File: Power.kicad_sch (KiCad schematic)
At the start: 39 parts, among them J7 Conn_01x02, Q1 AO3400A, Q2 AO3401A, Q3 AO3401A, U1 TPS62130

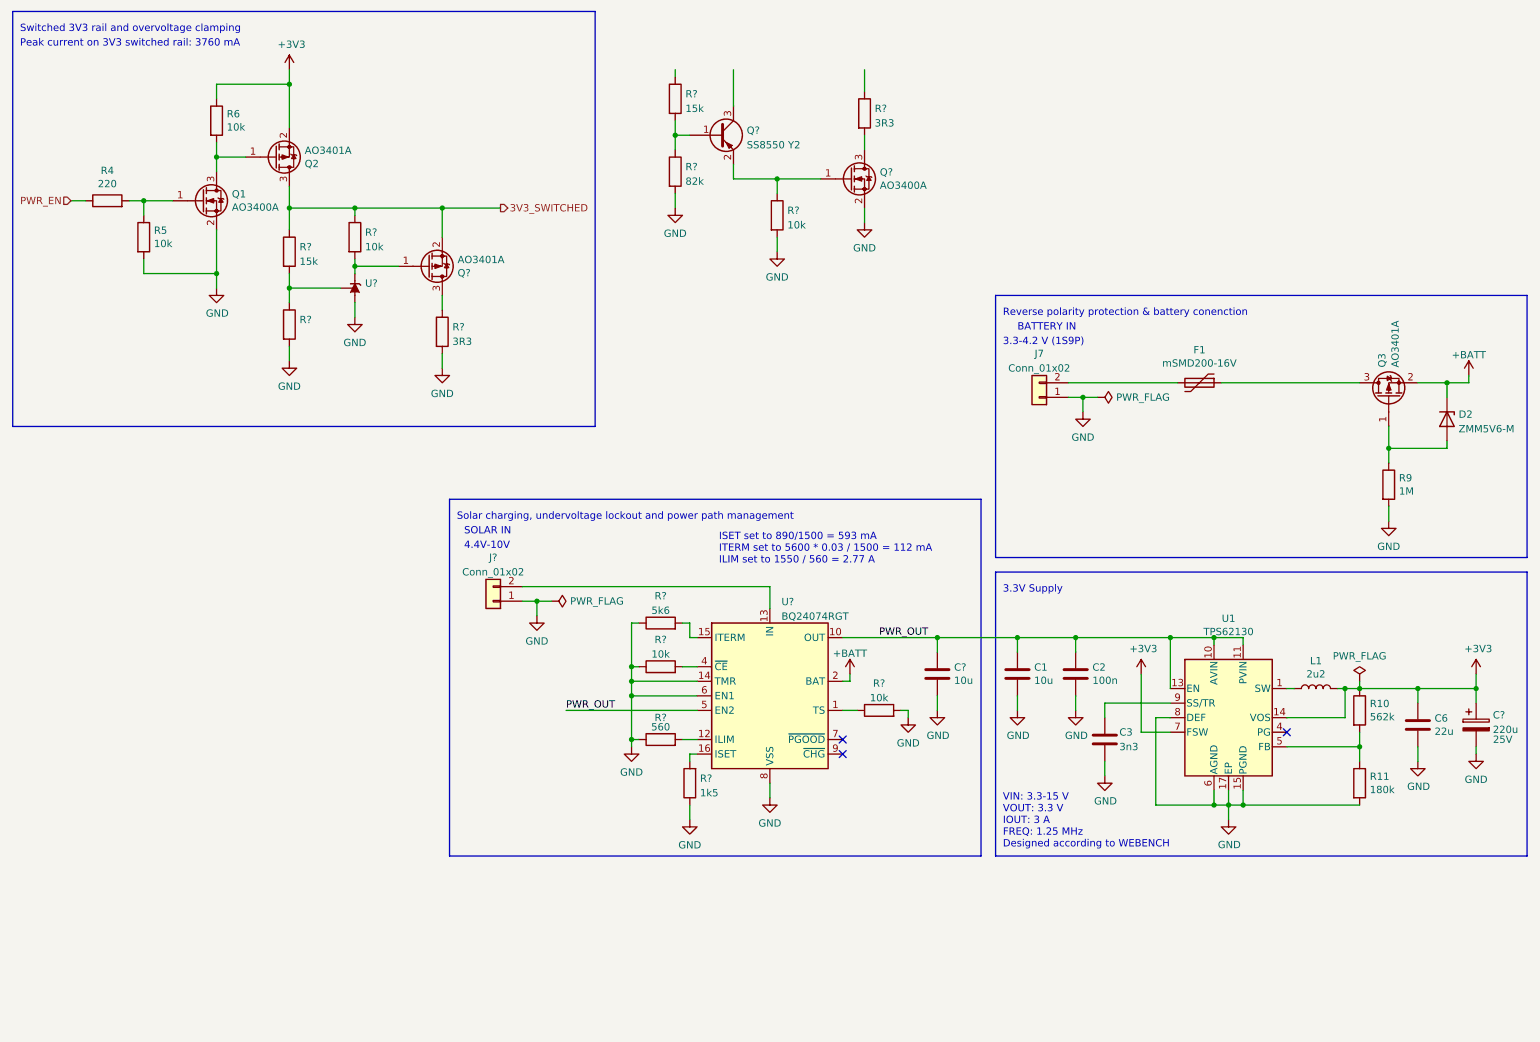
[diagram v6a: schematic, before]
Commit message: Finish rev. 2 schematic and begin PCB layout
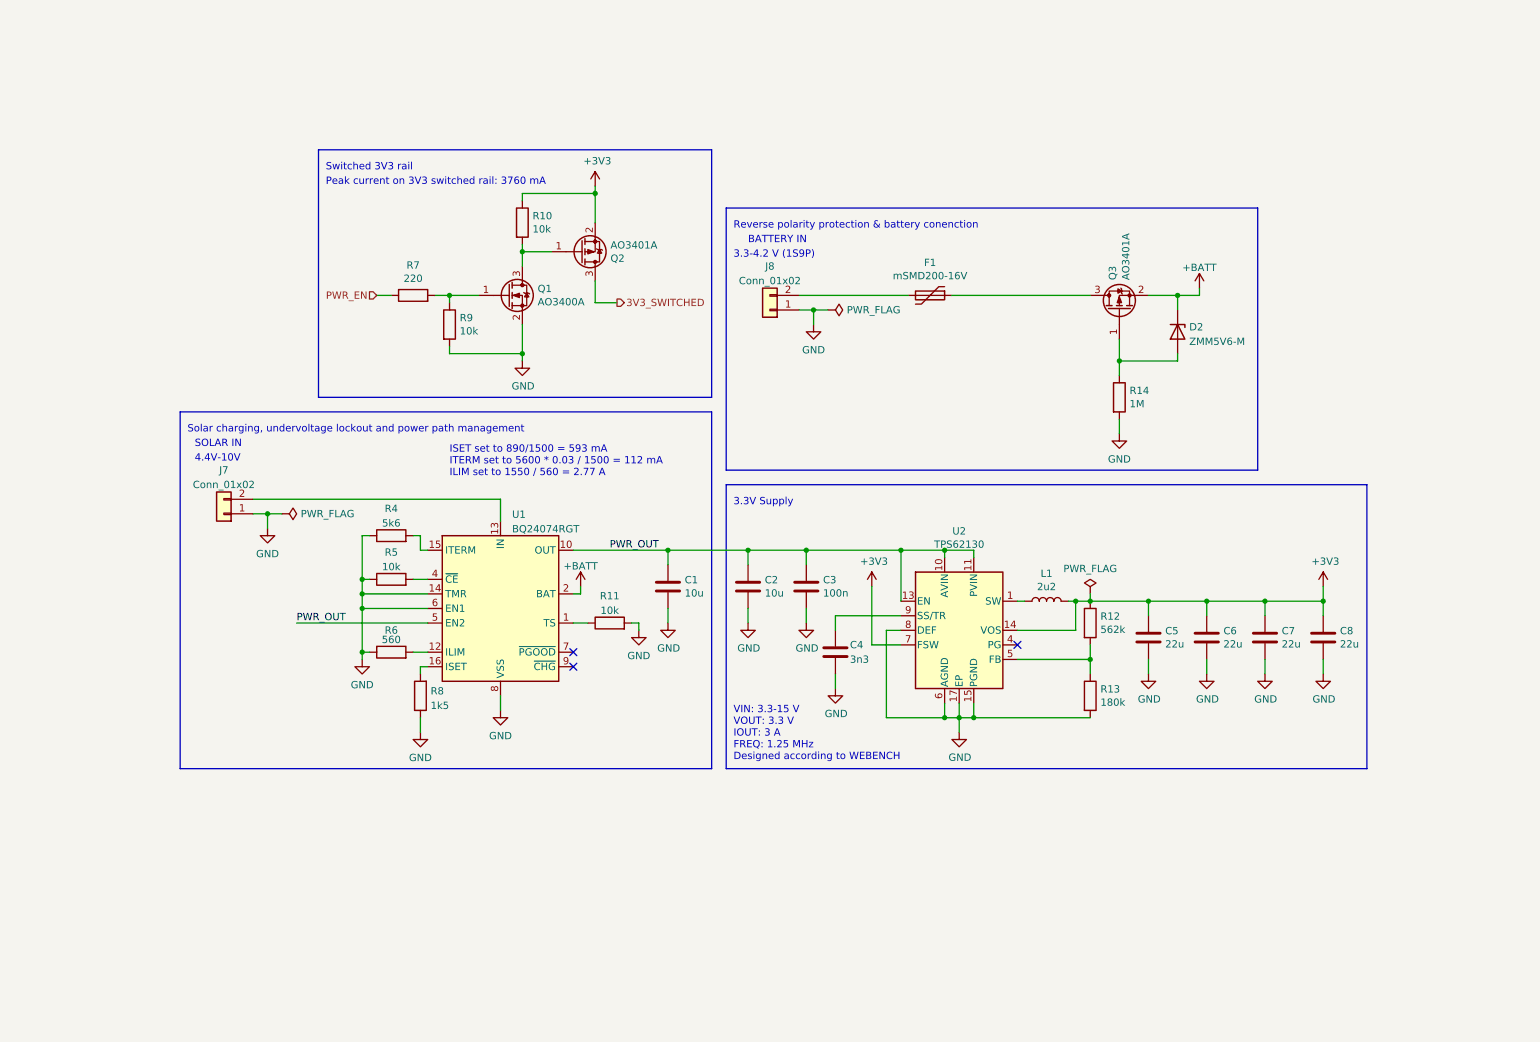
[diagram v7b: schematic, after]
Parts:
- removed C?: 220u, Capacitor_THT:CP_Radial_D8.0mm_P3.50mm, symbol Device:C_Polarized
- removed Q?: SS8550 Y2, symbol Device:Q_PNP_BEC
- removed Q?: AO3400A, Package_TO_SOT_SMD:SOT-23, symbol Transistor_FET:AO3400A
- removed Q?: AO3401A, Package_TO_SOT_SMD:SOT-23, symbol Transistor_FET:AO3401A
- removed R? (x2): 15k, symbol Device:R
- removed R? (x2): 3R3, symbol Device:R
- removed R? (x2): 10k, symbol Device:R
- removed R?: (no value), symbol Device:R
- removed R?: 82k, symbol Device:R
- removed U?: (no value), symbol Reference_Voltage:TL431PK
- added C6, C7, C8: 22u, Capacitor_SMD:C_0805_2012Metric, symbol Device:C
- R11, R5: renamed from R?; footprint (none) -> Resistor_SMD:R_0603_1608Metric; LCSC (none) -> C25804
- R4, R6, R8: renamed from R?; footprint (none) -> Resistor_SMD:R_0603_1608Metric
- gave numbers to parts that had none: 3
- renumbered C1 to C2, C2 to C3, C3 to C4, C6 to C5, J7 to J8, R6 to R10, R10 to R12, R11 to R13, R9 to R14, R4 to R7, R5 to R9, U1 to U2
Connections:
- net +3V3: now also C6.1, C7.1, C8.1
- net GND: now also C6.2, C7.2, C8.2
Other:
- note added: "Switched 3V3 rail"
- note removed: "Switched 3V3 rail and overvoltage clamping"
- moved on the sheet: C1, C2, C3, C4, C5, D2, F1, J7, J8, L1, Q1, Q2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

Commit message: Add 5V boost converter and begin redesign of PCB
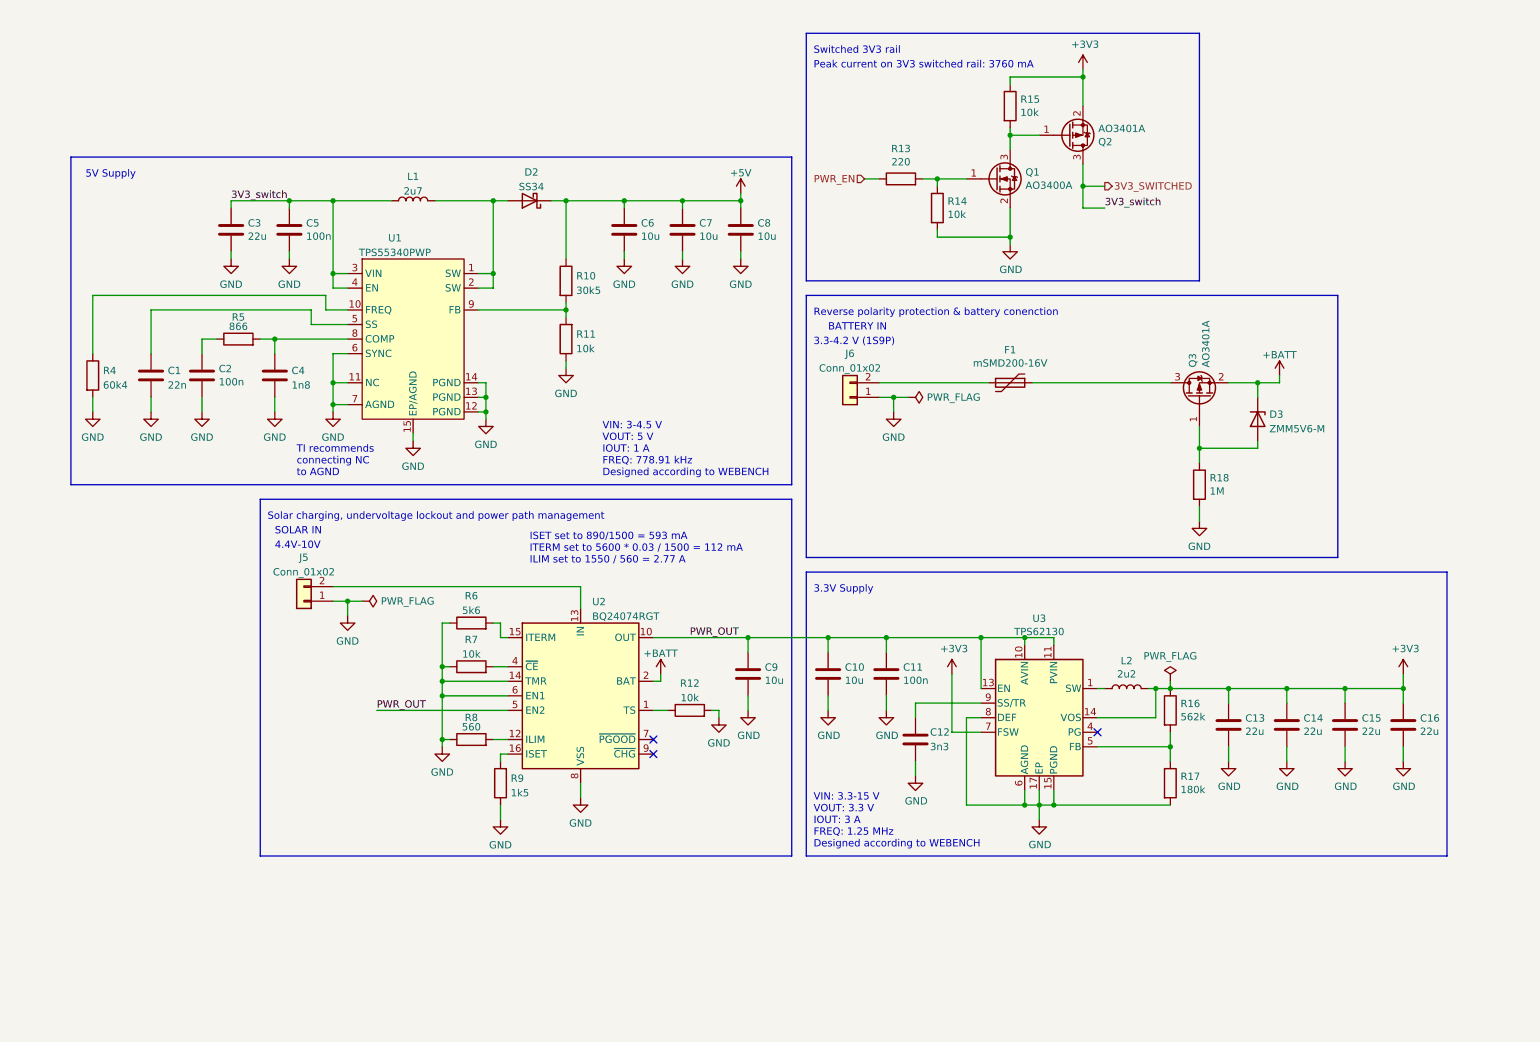
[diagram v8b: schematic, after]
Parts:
- added C1: 22n, Capacitor_SMD:C_0603_1608Metric, symbol Device:C
- added C2, C5: 100n, Capacitor_SMD:C_0603_1608Metric, symbol Device:C
- added C3: 22u, Capacitor_SMD:C_0805_2012Metric, symbol Device:C
- added C4: 1n8, Capacitor_SMD:C_0603_1608Metric, symbol Device:C
- added C6, C7, C8: 10u, Capacitor_SMD:C_0805_2012Metric, symbol Device:C
- added D2: SS34, Diode_SMD:D_SMA, symbol Device:D_Schottky
- added L1: 2u7, co2_sensor_node:PCD0504MT2R7, symbol Device:L
- added R10: 30k5, Resistor_SMD:R_0402_1005Metric, symbol Device:R
- added R11: 10k, Resistor_SMD:R_0603_1608Metric, symbol Device:R
- added R4: 60k4, Resistor_SMD:R_0402_1005Metric, symbol Device:R
- added R5: 866, Resistor_SMD:R_0402_1005Metric, symbol Device:R
- added U1: TPS55340PWP, Package_SO:HTSSOP-14-1EP_4.4x5mm_P0.65mm_EP3.4x5mm_Mask3x3.1mm_ThermalVias, symbol co2_sensor_node:TPS55340PWP
- renumbered C2 to C10, C3 to C11, C4 to C12, C5 to C13, C6 to C14, C7 to C15, C8 to C16, C1 to C9, D2 to D3, J7 to J5, J8 to J6, L1 to L2, R11 to R12, R7 to R13, R9 to R14, R10 to R15, R12 to R16, R13 to R17, R14 to R18, R4 to R6, R5 to R7, R6 to R8, R8 to R9, U1 to U2, U2 to U3
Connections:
- net 3V3_SWITCHED: now also C3.1, C5.1, L1.1, U1.3 (VIN), U1.4 (EN)
- net GND: now also C1.2, C2.2, C3.2, C4.2, C5.2, C6.2, C7.2, C8.2, R11.1, R4.2, U1.11 (NC), U1.12 (PGND), U1.13 (PGND), U1.14 (PGND), U1.15 (EP/AGND), U1.6 (SYNC), U1.7 (AGND)
- new net: D2.2 (A), L1.2, U1.1 (SW), U1.2 (SW)
- new net: C4.1, R5.2, U1.8 (COMP)
- new net: C2.1, R5.1
- new net: R4.1, U1.10 (FREQ)
- new net: C1.1, U1.5 (SS)
- new net: R10.2, R11.2, U1.9 (FB)
- new net +5V: C6.1, C7.1, C8.1, D2.1 (K), R10.1
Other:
- note added: "5V Supply"
- note added: "TI recommends connecting NC to AGND"
- note added: "VIN: 3-4.5 V VOUT: 5 V IOUT: 1 A FREQ: 778.91 kHz Designed according to WEBENCH"
- moved on the sheet: C10, C11, C12, C13, C14, C15, C16, C9, D3, F1, J5, J6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
